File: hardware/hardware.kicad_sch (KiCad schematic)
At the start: 15 parts, among them J1 Conn_01x02_Pin, U1 ESP32-S3-WROOM-1, U2 LM2596S-ADJ, U3 AMS1117-3.3, U4 SIM800L-CORE

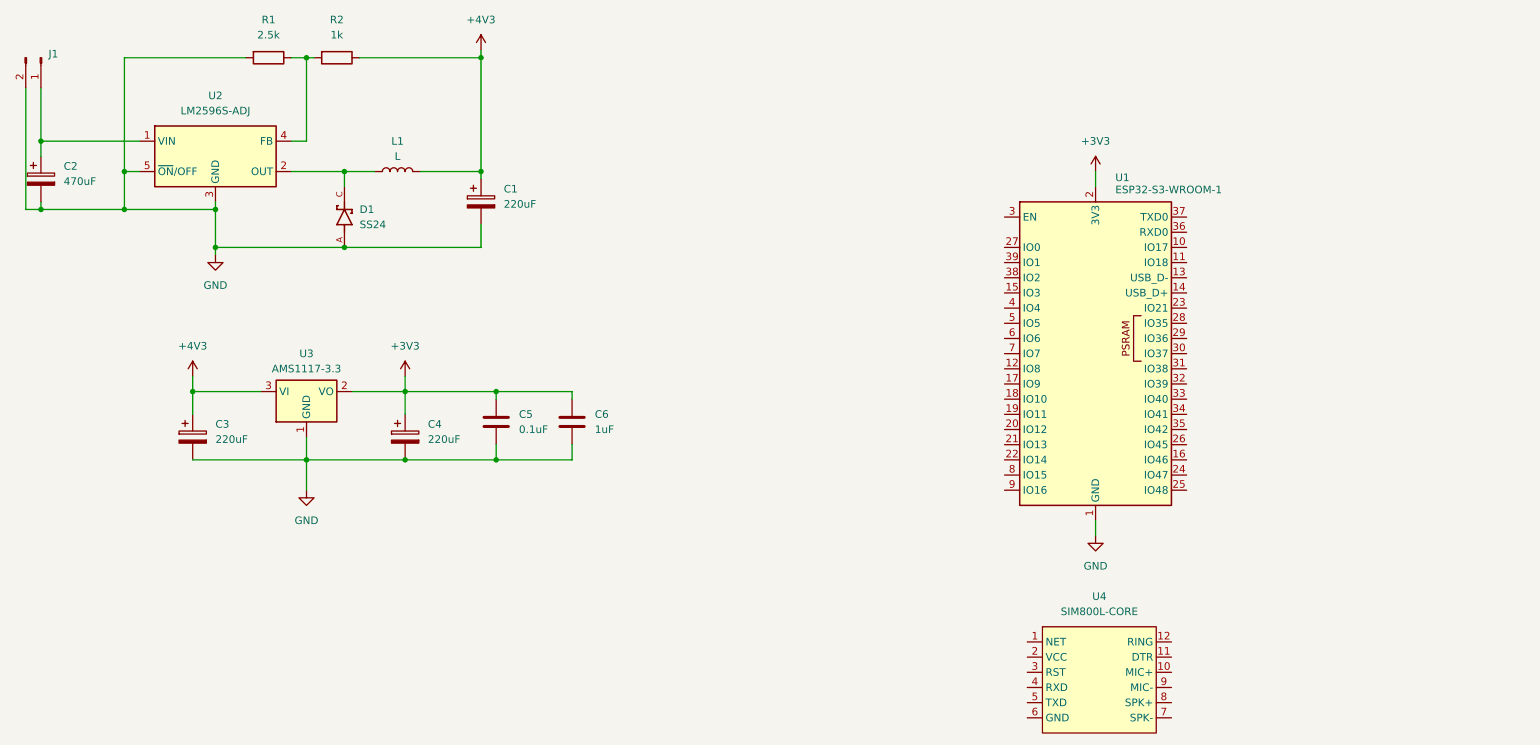
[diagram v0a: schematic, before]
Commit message: upgrading circuits and power supplies circuit
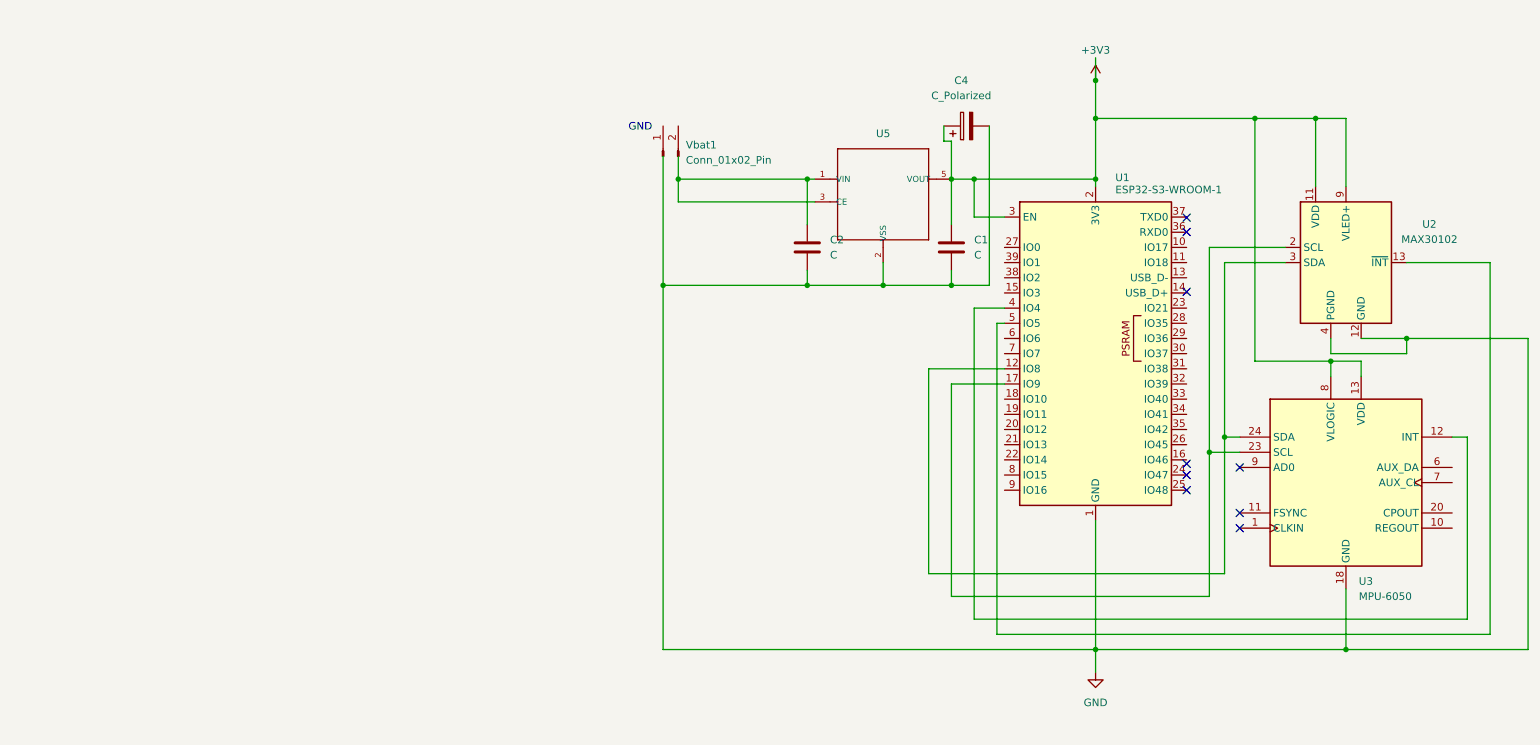
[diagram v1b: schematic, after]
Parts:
- removed C1: 220uF, Capacitor_SMD:CP_Elec_10x12.5, symbol Device:C_Polarized
- removed C2: 470uF, Capacitor_SMD:CP_Elec_10x12.5, symbol Device:C_Polarized
- removed C3: 220uF, Capacitor_SMD:CP_Elec_10x7.7, symbol Device:C_Polarized
- removed C5: 0.1uF, Capacitor_SMD:C_0603_1608Metric, symbol Device:C
- removed C6: 1uF, Capacitor_SMD:C_0603_1608Metric, symbol Device:C
- removed D1: SS24, SS24:DIOM4336X265N, symbol SS24:SS24
- removed J1: Conn_01x02_Pin, Connector:JWT_A3963_1x02_P3.96mm_Vertical, symbol Connector:Conn_01x02_Pin
- removed L1: L, Inductor_SMD:L_Abracon_ASPI-0630LR, symbol Device:L
- removed R1: 2.5k, Resistor_SMD:R_1206_3216Metric, symbol Device:R
- removed R2: 1k, Resistor_SMD:R_1206_3216Metric, symbol Device:R
- removed U2: LM2596S-ADJ, Package_TO_SOT_SMD:TO-263-5_TabPin3, symbol Regulator_Switching:LM2596S-ADJ
- removed U3: AMS1117-3.3, Package_TO_SOT_SMD:SOT-223-3_TabPin2, symbol Regulator_Linear:AMS1117-3.3
- removed U4: SIM800L-CORE, symbol sim800l-core:SIM800L-CORE
- added C1, C2: C, Capacitor_SMD:C_0805_2012Metric, symbol Device:C
- added U2: MAX30102, Connector_PinHeader_2.54mm:PinHeader_1x07_P2.54mm_Vertical_SMD_Pin1Left, symbol Sensor:MAX30102
- added U3: MPU-6050, Connector_PinHeader_2.54mm:PinHeader_1x08_P2.54mm_Vertical, symbol Sensor_Motion:MPU-6050
- added U5: XC6204B332MR-SOT23-5, Package_TO_SOT_SMD:SOT-23-5, symbol PMIC-XC6204B332MR_SOT23-5_:PMIC-XC6204B332MR_SOT23-5_
- added Vbat1: Conn_01x02_Pin, Connector_PinHeader_2.54mm:PinHeader_1x02_P2.54mm_Vertical_SMD_Pin1Left, symbol Connector:Conn_01x02_Pin
- C4: value 220uF -> C_Polarized; footprint Capacitor_SMD:CP_Elec_10x7.7 -> Capacitor_SMD:CP_Elec_8x10.5
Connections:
- net +3V3: now also U1.3 (EN), C1.1, U2.10 (VLED+), U2.11 (VDD), U2.9 (VLED+), U3.13 (VDD), U3.8 (VLOGIC), U5.5 (VOUT)
- net GND: now also C1.2, C2.2, U2.12 (GND), U2.4 (PGND), U3.18 (GND), U5.2 (VSS)
- net at U1.12 (IO8): now also U2.3 (SDA), U3.24 (SDA)
- net at U1.17 (IO9): now also U2.2 (SCL), U3.23 (SCL)
- net at U1.4 (IO4): now also U3.12 (INT)
- net at U1.5 (IO5): now also U2.13 (~{INT})
- new net: C2.1, U5.1 (VIN), U5.3 (CE)
- no-connect marks 0 -> 9
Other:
- note added: "GND"
